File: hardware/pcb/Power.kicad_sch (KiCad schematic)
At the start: 15 parts, among them J2 USB_B_Micro, Q1 Q_PNP_CBE, Q2 Q_NPN_CBE, SW1 SW_SPST, U1 XC6808A4D28R-G, U3 NCP160AMX330TBG

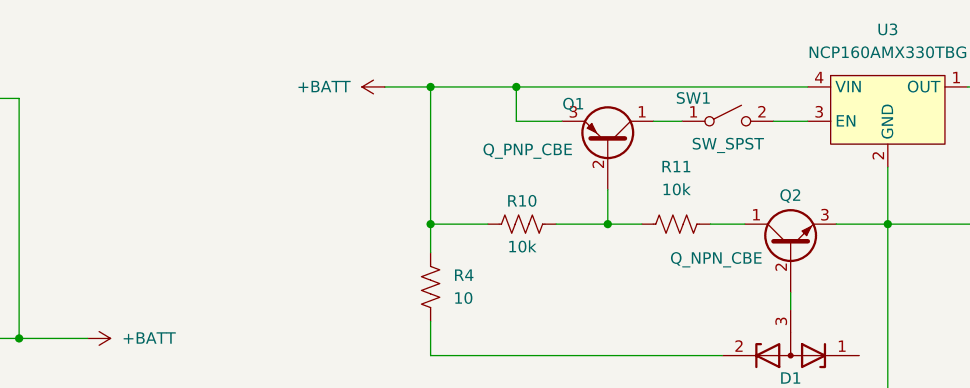
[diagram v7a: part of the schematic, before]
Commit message: Rework overdischarge protection
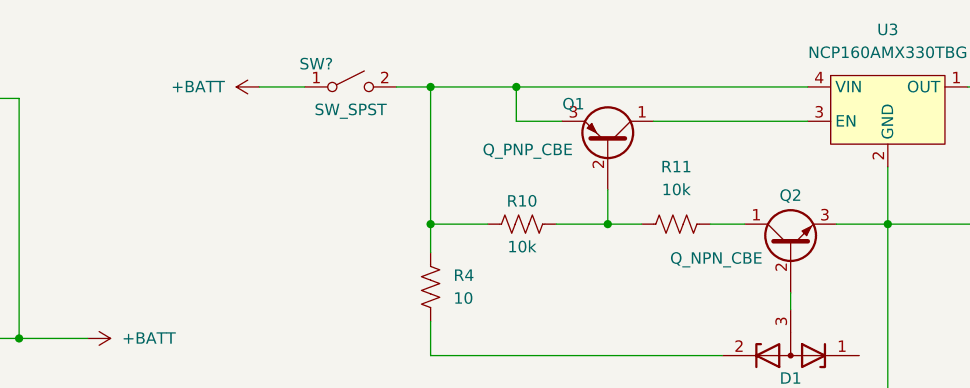
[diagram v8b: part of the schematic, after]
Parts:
- removed SW1: SW_SPST, symbol Switch:SW_SPST
- added SW?: SW_SPST, symbol Switch:SW_SPST
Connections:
- net +BATT: now also SW?.1 (A); no longer Q1.3 (E), R10.1, R4.1, U3.4 (VIN)
- net at U3.3 (EN): now also Q1.1 (C)
- new net: Q1.3 (E), R10.1, R4.1, SW?.2 (B), U3.4 (VIN)
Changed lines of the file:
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@@
   (junction (at 180.34 96.52) (diameter 0) (color 0 0 0 0)
   )
+  (junction (at 83.82 93.98) (diameter 0) (color 0 0 0 0)
+  )
+  (junction (at 83.82 109.22) (diameter 0) (color 0 0 0 0)
+  )
+  (junction (at 200.025 96.52) (diameter 0) (color 0 0 0 0)
+  )
+  (junction (at 243.84 81.28) (diameter 0) (color 0 0 0 0)
+  )
   (junction (at 180.34 81.28) (diameter 0) (color 0 0 0 0)
   )
-  (junction (at 83.82 93.98) (diameter 0) (color 0 0 0 0)
-  )
-  (junction (at 83.82 109.22) (diameter 0) (color 0 0 0 0)
-  )
-  (junction (at 200.025 96.52) (diameter 0) (color 0 0 0 0)
-  )
-  (junction (at 243.84 81.28) (diameter 0) (color 0 0 0 0)
-  )
   (wire (pts (xy 231.14 96.52) (xy 231.14 118.11))
     (stroke (width 0) (type default) (color 0 0 0 0))
@@
     (stroke (width 0) (type default) (color 0 0 0 0))
   )
-  (wire (pts (xy 205.105 85.09) (xy 208.28 85.09))
-    (stroke (width 0) (type default) (color 0 0 0 0))
-  )
   (wire (pts (xy 180.34 96.52) (xy 180.34 99.695))
     (stroke (width 0) (type default) (color 0 0 0 0))
@@
     (stroke (width 0) (type default) (color 0 0 0 0))
   )
+  (wire (pts (xy 176.53 81.28) (xy 180.34 81.28))
+    (stroke (width 0) (type default) (color 0 0 0 0))
+  )
   (wire (pts (xy 83.82 87.63) (xy 83.82 93.98))
     (stroke (width 0) (type default) (color 0 0 0 0))
@@
     (stroke (width 0) (type default) (color 0 0 0 0))
   )
-  (wire (pts (xy 218.44 85.09) (xy 222.25 85.09))
+  (wire (pts (xy 205.105 85.09) (xy 222.25 85.09))
     (stroke (width 0) (type default) (color 0 0 0 0))
   )
@@
     (stroke (width 0) (type default) (color 0 0 0 0))
   )
+  (wire (pts (xy 161.29 81.28) (xy 166.37 81.28))
+    (stroke (width 0) (type default) (color 0 0 0 0))
+  )
   (wire (pts (xy 100.33 109.22) (xy 118.11 109.22))
     (stroke (width 0) (type default) (color 0 0 0 0))
@@
   )
   (wire (pts (xy 220.345 104.14) (xy 220.345 106.045))
-    (stroke (width 0) (type default) (color 0 0 0 0))
-  )
-  (wire (pts (xy 175.26 81.28) (xy 180.34 81.28))
     (stroke (width 0) (type default) (color 0 0 0 0))
   )
@@
     (pin "2")
   )
-  (symbol (lib_id "power:+BATT") (at 175.26 81.28 90) (unit 1)
-    (in_bom yes) (on_board yes) (fields_autoplaced)
-    (property "Reference" "#PWR0110" (id 0) (at 179.07 81.28 0)
-      (effects (font (size 1.27 1.27)) hide)
-    )
-    (property "Value" "+BATT" (id 1) (at 171.45 81.2799 90)
+  (symbol (lib_id "Switch:SW_SPST") (at 171.45 81.28 0) (unit 1)
+    (in_bom yes) (on_board yes)
+    (property "Reference" "SW?" (id 0) (at 167.64 78.74 0))
+    (property "Value" "SW_SPST" (id 1) (at 171.45 83.82 0))
+    (property "Footprint" "" (id 2) (at 171.45 81.28 0)
+      (effects (font (size 1.27 1.27)) hide)
+    )
+    (property "Datasheet" "~" (id 3) (at 171.45 81.28 0)
+      (effects (font (size 1.27 1.27)) hide)
+    )
+    (pin "1")
+    (pin "2")
+  )
+  (symbol (lib_id "power:+BATT") (at 161.29 81.28 90) (unit 1)
+    (in_bom yes) (on_board yes) (fields_autoplaced)
+    (property "Reference" "#PWR0110" (id 0) (at 165.1 81.28 0)
+      (effects (font (size 1.27 1.27)) hide)
+    )
+    (property "Value" "+BATT" (id 1) (at 157.48 81.2799 90)
       (effects (font (size 1.27 1.27)) (justify left))
     )
-    (property "Footprint" "" (id 2) (at 175.26 81.28 0)
-      (effects (font (size 1.27 1.27)) hide)
-    )
-    (property "Datasheet" "" (id 3) (at 175.26 81.28 0)
+    (property "Footprint" "" (id 2) (at 161.29 81.28 0)
+      (effects (font (size 1.27 1.27)) hide)
+    )
+    (property "Datasheet" "" (id 3) (at 161.29 81.28 0)
       (effects (font (size 1.27 1.27)) hide)
     )
@@
     (pin "3")
   )
-  (symbol (lib_id "Switch:SW_SPST") (at 213.36 85.09 0) (unit 1)
-    (in_bom yes) (on_board yes)
-    (property "Reference" "SW1" (id 0) (at 209.55 82.55 0))
-    (property "Value" "SW_SPST" (id 1) (at 213.36 87.63 0))
-    (property "Footprint" "" (id 2) (at 213.36 85.09 0)
-      (effects (font (size 1.27 1.27)) hide)
-    )
-    (property "Datasheet" "~" (id 3) (at 213.36 85.09 0)
-      (effects (font (size 1.27 1.27)) hide)
-    )
-    (pin "1")
-    (pin "2")
-  )
   (symbol (lib_id "Device:C") (at 243.84 88.9 0) (unit 1)
